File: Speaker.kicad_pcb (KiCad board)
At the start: 2 copper layers, 66 parts, among them J1 USB_C_Receptacle_USB2.0_16P, SW1 SW_Push, SW2 Volume Up, SW3 Volume Down, SW4 Play/Pause, SW5 Power Switch, U1 TPS61088RHLT, U2 MCP73871, U3 AP2112K-3.3, U4 MAX17048G_T10, U5 USBLC6-2SC6, U6 CH340X, U7 ESP32-WROOM-32, U8 MAX98357A

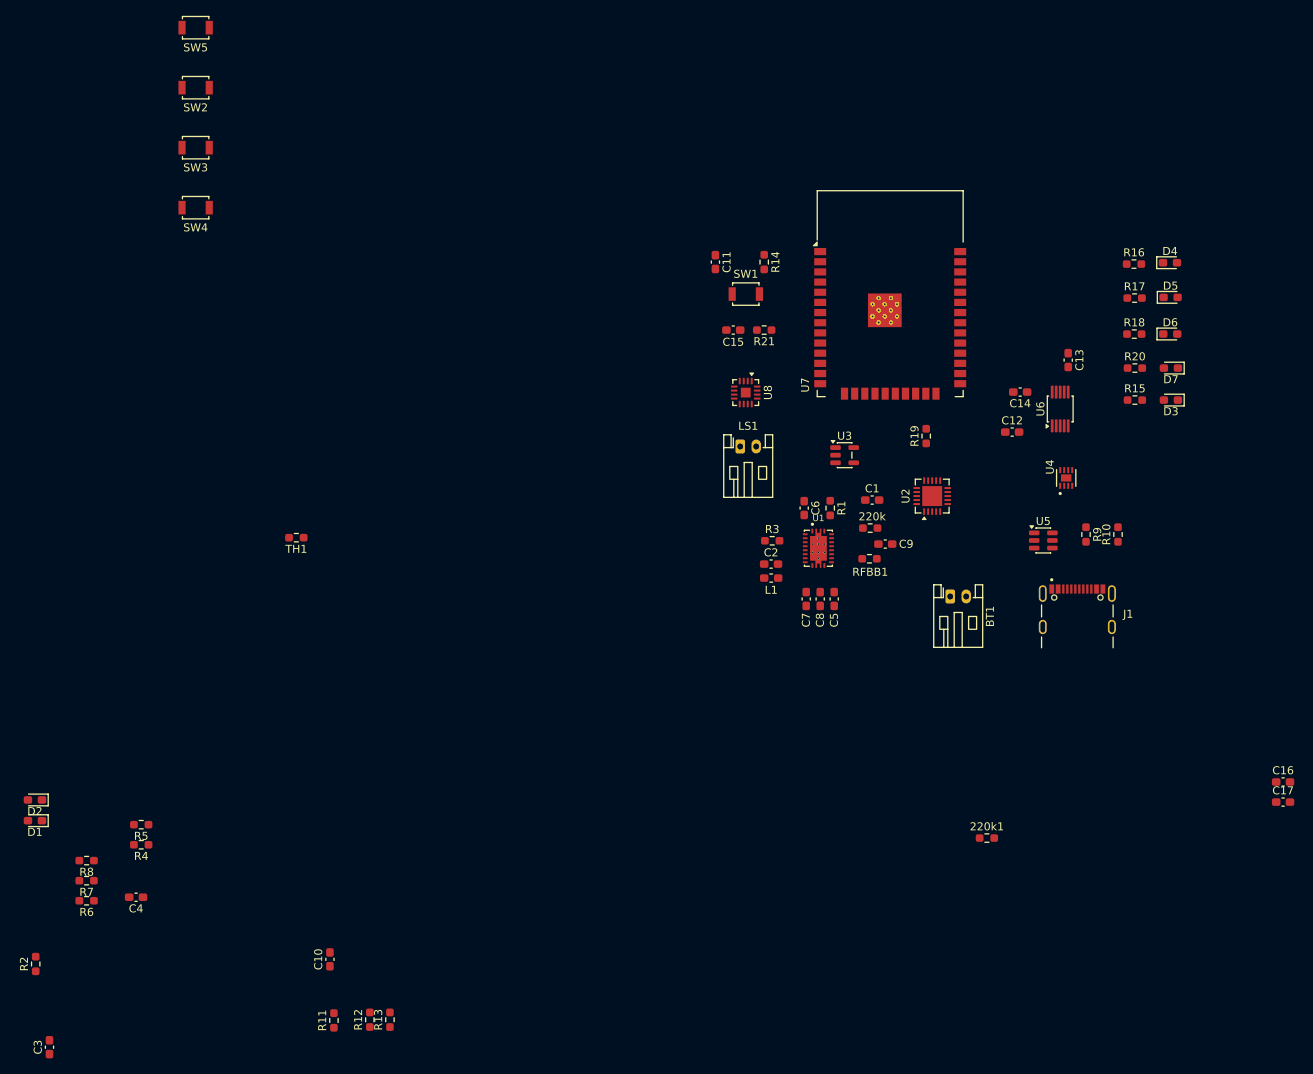
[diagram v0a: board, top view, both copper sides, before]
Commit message: Update the USB-C symbol to match the actual part
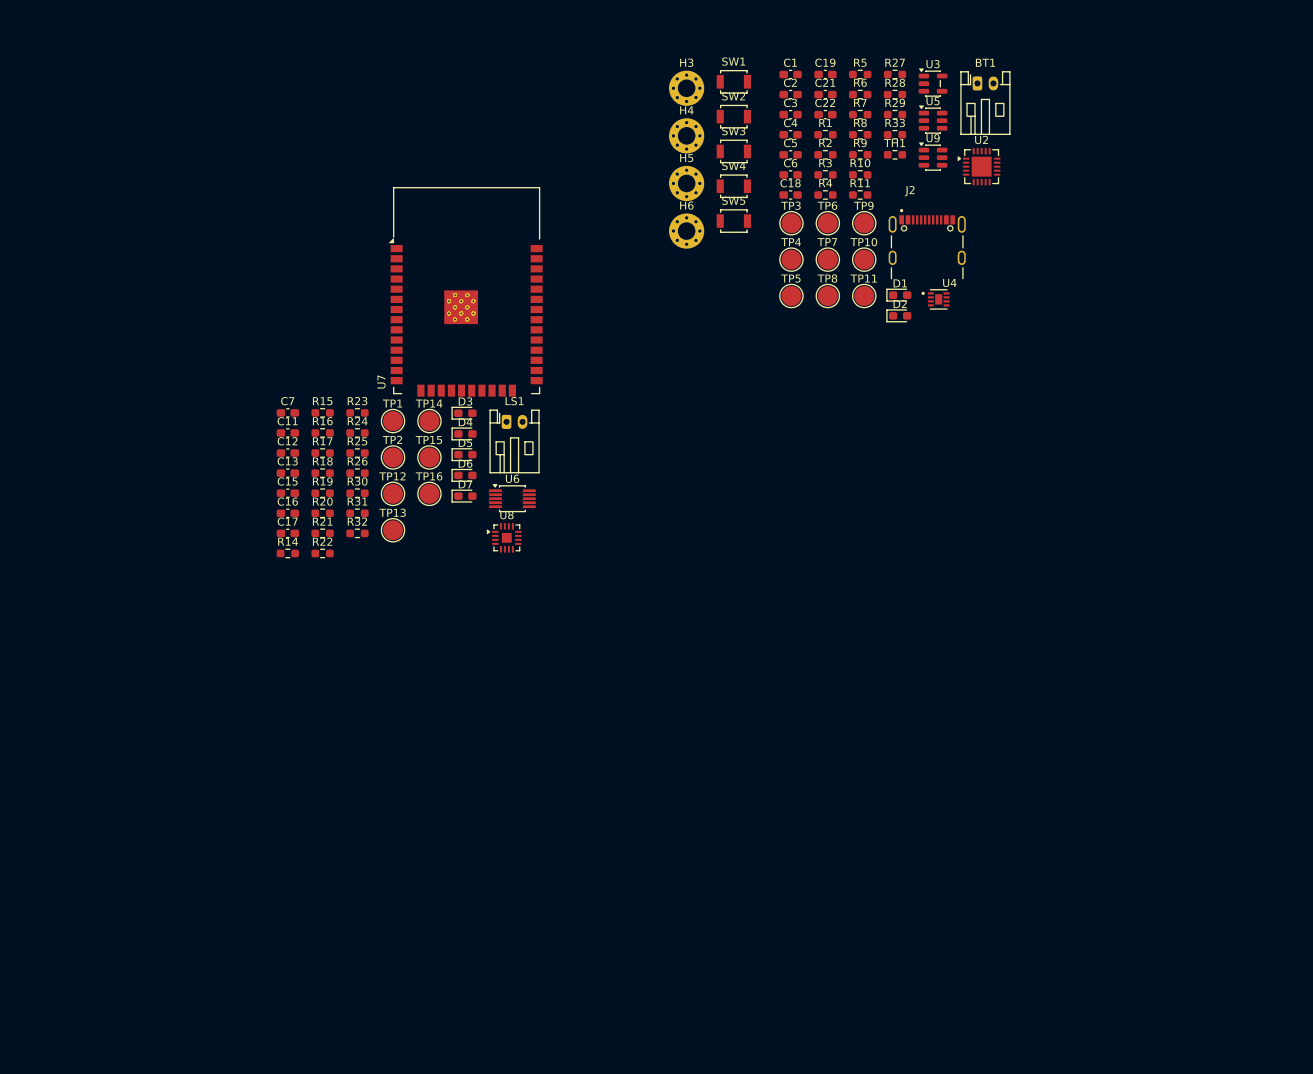
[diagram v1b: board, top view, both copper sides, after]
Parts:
- removed 220k, 220k1: RFB, Resistor_SMD:R_0603_1608Metric_Pad0.98x0.95mm_HandSolder
- removed C10: 100nF, Capacitor_SMD:C_0603_1608Metric_Pad1.08x0.95mm_HandSolder
- removed C14, C8: 0.1uF, Capacitor_SMD:C_0603_1608Metric_Pad1.08x0.95mm_HandSolder
- removed C9: 47uF, Capacitor_SMD:C_0603_1608Metric_Pad1.08x0.95mm_HandSolder
- removed J1: USB_C_Receptacle_USB2.0_16P, UJ20-C-H-G-SMT-1-P16-TR:SAMESKY_UJ20-C-H-G-SMT-1-P16-TR
- removed L1: 1.2uH, Inductor_SMD:L_0603_1608Metric_Pad1.05x0.95mm_HandSolder
- removed R12, R13: 5.1k, Resistor_SMD:R_0603_1608Metric_Pad0.98x0.95mm_HandSolder
- removed RFBB1: 70k, Resistor_SMD:R_0603_1608Metric_Pad0.98x0.95mm_HandSolder
- removed U1: TPS61088RHLT, TPS61088RHLT:IC_MSP430FR2522IRHLR
- added C18: 1uF, Capacitor_SMD:C_0603_1608Metric_Pad1.08x0.95mm_HandSolder, F.Cu at (128.3, 66.8)
- added C19: 1uF, Capacitor_SMD:C_0603_1608Metric_Pad1.08x0.95mm_HandSolder, F.Cu at (132.7, 51.7)
- added C21: 100pF, Capacitor_SMD:C_0603_1608Metric_Pad1.08x0.95mm_HandSolder, F.Cu at (132.7, 54.2)
- added C22: 100nF, Capacitor_SMD:C_0603_1608Metric_Pad1.08x0.95mm_HandSolder, F.Cu at (132.7, 56.8)
- added H3: MountingHole, MountingHole:MountingHole_2.2mm_M2_Pad_Via, F.Cu at (115.3, 53.5)
- added H4: MountingHole, MountingHole:MountingHole_2.2mm_M2_Pad_Via, F.Cu at (115.3, 59.4)
- added H5: MountingHole, MountingHole:MountingHole_2.2mm_M2_Pad_Via, F.Cu at (115.3, 65.4)
- added H6: MountingHole, MountingHole:MountingHole_2.2mm_M2_Pad_Via, F.Cu at (115.3, 71.3)
- added J2: UJ20-C-H-G-SMT-1-P16-TR, UJ20-C-H-G-SMT-1-P16-TR:SAMESKY_UJ20-C-H-G-SMT-1-P16-TR, F.Cu at (145.4, 77.3)
- added R22: 0, Resistor_SMD:R_0603_1608Metric_Pad0.98x0.95mm_HandSolder, F.Cu at (69.8, 111.6)
- added R23: 0, Resistor_SMD:R_0603_1608Metric_Pad0.98x0.95mm_HandSolder, F.Cu at (74.2, 94.0)
- added R24: 0, Resistor_SMD:R_0603_1608Metric_Pad0.98x0.95mm_HandSolder, F.Cu at (74.2, 96.5)
- added R25: 0, Resistor_SMD:R_0603_1608Metric_Pad0.98x0.95mm_HandSolder, F.Cu at (74.2, 99.1)
- added R26: 0, Resistor_SMD:R_0603_1608Metric_Pad0.98x0.95mm_HandSolder, F.Cu at (74.2, 101.6)
- added R27: 0, Resistor_SMD:R_0603_1608Metric_Pad0.98x0.95mm_HandSolder, F.Cu at (141.4, 51.7)
- added R28: 0, Resistor_SMD:R_0603_1608Metric_Pad0.98x0.95mm_HandSolder, F.Cu at (141.4, 54.2)
- added R29: 0, Resistor_SMD:R_0603_1608Metric_Pad0.98x0.95mm_HandSolder, F.Cu at (141.4, 56.8)
- added R30: 0, Resistor_SMD:R_0603_1608Metric_Pad0.98x0.95mm_HandSolder, F.Cu at (74.2, 104.1)
- added R31: 0, Resistor_SMD:R_0603_1608Metric_Pad0.98x0.95mm_HandSolder, F.Cu at (74.2, 106.6)
- added R32: 0, Resistor_SMD:R_0603_1608Metric_Pad0.98x0.95mm_HandSolder, F.Cu at (74.2, 109.1)
- added R33: 5.1k, Resistor_SMD:R_0603_1608Metric_Pad0.98x0.95mm_HandSolder, F.Cu at (141.4, 59.3)
- added TP1: TP_UART_TX, TestPoint:TestPoint_Pad_D2.5mm, F.Cu at (78.6, 95.1)
- added TP10: TP_VREG3.3, TestPoint:TestPoint_Pad_D2.5mm, F.Cu at (137.5, 74.9)
- added TP11: TP_VSYS_LDO, TestPoint:TestPoint_Pad_D2.5mm, F.Cu at (137.5, 79.4)
- added TP12: TP_D-, TestPoint:TestPoint_Pad_D2.5mm, F.Cu at (78.6, 104.2)
- added TP13: TP_D+, TestPoint:TestPoint_Pad_D2.5mm, F.Cu at (78.6, 108.7)
- added TP14: TP_DIN, TestPoint:TestPoint_Pad_D2.5mm, F.Cu at (83.2, 95.1)
- added TP15: TP_DIN, TestPoint:TestPoint_Pad_D2.5mm, F.Cu at (83.2, 99.6)
- added TP16: TP_BCLK, TestPoint:TestPoint_Pad_D2.5mm, F.Cu at (83.2, 104.2)
- added TP2: TP_UART_RX, TestPoint:TestPoint_Pad_D2.5mm, F.Cu at (78.6, 99.6)
- added TP3: TP_Charging, TestPoint:TestPoint_Pad_D2.5mm, F.Cu at (128.4, 70.3)
- added TP4: TP_VSYS, TestPoint:TestPoint_Pad_D2.5mm, F.Cu at (128.4, 74.9)
- added TP5: TP_VDD, TestPoint:TestPoint_Pad_D2.5mm, F.Cu at (128.4, 79.4)
- added TP6: TP_VBAT+, TestPoint:TestPoint_Pad_D2.5mm, F.Cu at (133.0, 70.3)
- added TP7: TP_FG_SDA, TestPoint:TestPoint_Pad_D2.5mm, F.Cu at (133.0, 74.9)
- added TP8: TP_FG_SCL, TestPoint:TestPoint_Pad_D2.5mm, F.Cu at (133.0, 79.4)
- added TP9: TP_FG_ALRT, TestPoint:TestPoint_Pad_D2.5mm, F.Cu at (137.5, 70.3)
- added U9: USBLC6-2SC6, Package_TO_SOT_SMD:SOT-23-6, F.Cu at (146.1, 62.1)
- C1: value 39pF -> 1uF
- C2: value 0.1uF -> 100pF
- C3: value 1nF -> 100nF
- C4: value 4.7u -> 4.7uF
- C5: value 47nF -> 4.7uF
- C6: value 2.2uF -> 0.1uF
- C7: value 10uF -> 0.1uF
- R1: value 23.7k -> 330k
- R2: value 243K -> 110k
- R3: value 322K -> 5.1k
- R5: value 5k -> 10k
- R6: value 10k -> 470
- moved C3 148.9 mm to (128.3, 56.8), turned to 0 degrees
- moved R2 141.3 mm to (132.7, 61.8), turned to 0 degrees
- moved R6 139.7 mm to (137.0, 54.2), turned to 0 degrees
- moved R7 136.1 mm to (137.0, 56.8), turned to 0 degrees
- moved R8 132.6 mm to (137.0, 59.3), turned to 0 degrees
- moved R5 129.9 mm to (137.0, 51.7), turned to 0 degrees
- moved C16 128.9 mm to (65.5, 106.6)
- moved C17 128.9 mm to (65.5, 109.1)
- moved D1 126.5 mm to (142.0, 79.3), turned to 0 degrees
- moved C4 125.6 mm to (128.3, 59.3), turned to 0 degrees
- moved D2 123.9 mm to (142.0, 81.9), turned to 0 degrees
- moved R11 122.4 mm to (137.0, 66.8), turned to 0 degrees
- moved R4 117.9 mm to (132.7, 66.8), turned to 0 degrees
- moved R16 103.6 mm to (69.8, 96.5)
- moved R17 103.3 mm to (69.8, 99.1)
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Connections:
- C1 pad 1: Net-(U1-COMP) -> GND
- C1 pad 2: GND -> VDD
- C16 pad 2: VREG_5V -> VREG_3.3V
- C17 pad 2: VREG_5V -> VREG_3.3V
- C2 pad 1: Net-(C2-Pad1) -> GND
- C2 pad 2: Net-(U1-BOOT) -> VDD
- C3 pad 1: Net-(C3-Pad1) -> GND
- C3 pad 2: GND -> VDD
- C5 pad 1: Net-(U1-SS) -> VSYS
- C6 pad 1: GND -> VBAT+
- C6 pad 2: Net-(U1-VCC) -> GND
- C7 pad 2: VSYS -> VREG_3.3V
- D1 pad 2: Net-(D1-A) -> VDD
- D2 pad 2: Net-(D2-A) -> VDD
- R1 pad 1: Net-(U1-COMP) -> VDD
- R1 pad 2: Net-(C3-Pad1) -> Net-(U2-VPCC)
- R2 pad 1: Net-(U1-ILIM) -> GND
- R2 pad 2: GND -> Net-(U2-VPCC)
- R3 pad 1: Net-(C2-Pad1) -> GND
- R7 pad 1: Net-(D1-A) -> Net-(U2-STAT1/~{LBO})
- R7 pad 2: VREG_3.3V -> Net-(D1-K)
- R8 pad 1: Net-(D2-A) -> Net-(U2-STAT2)
- R8 pad 2: VREG_3.3V -> Net-(D2-K)
- U2 pad 2: VDD -> Net-(U2-VPCC)
- U2 pad 7: Net-(D2-K) -> Net-(U2-STAT2)
- U2 pad 8: Net-(D1-K) -> Net-(U2-STAT1/~{LBO})
- U3 pad 1: VREG_5V -> VSYS
- U3 pad 3: VREG_5V -> VSYS
- U4 pad 3: VREG_3.3V -> VBAT+
- U6 pad 1: D+ -> Net-(U6-UD+)
- U6 pad 2: D- -> Net-(U6-UD-)
- U6 pad 7: VREG_5V -> Net-(U6-V3)
- U7 pad 9: unconnected-(U7-IO33-Pad9) -> /MCU/AMP_SDM
- U8 pad 4: unconnected-(U8-~{SD_MODE}-Pad4) -> /MCU/AMP_SDM
- U8 pad 7: VREG_5V -> VREG_3.3V
- U8 pad 8: VREG_5V -> VREG_3.3V

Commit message: Put component families together on PCB
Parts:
- added C8: 1nF, Capacitor_SMD:C_0603_1608Metric_Pad1.08x0.95mm_HandSolder, F.Cu at (70.0, 38.6)
- TP1, TP10, TP11, TP12, TP13, TP14, TP15, TP16, TP2, TP3, TP4, TP5, TP6, TP7, TP8, TP9: footprint TestPoint:TestPoint_Pad_D2.5mm -> TestPoint:TestPoint_Pad_D1.5mm
- moved R20 198.7 mm to (259.5, 47.6)
- moved R18 196.9 mm to (259.8, 49.9), turned to 180 degrees
- moved R17 195.6 mm to (259.8, 52.4), turned to 180 degrees
- moved R16 194.5 mm to (259.8, 54.9), turned to 180 degrees
- moved R15 193.4 mm to (259.8, 57.4), turned to 180 degrees
- moved D7 184.8 mm to (263.5, 47.6), turned to 180 degrees
- moved D6 183.4 mm to (263.5, 49.6), turned to 180 degrees
- moved D5 182.0 mm to (263.5, 52.2), turned to 180 degrees
- moved D4 180.7 mm to (263.5, 54.8), turned to 180 degrees
- moved D3 179.6 mm to (263.5, 57.4), turned to 180 degrees
- moved R19 175.9 mm to (240.8, 62.9), turned to -90 degrees
- moved R14 170.4 mm to (221.8, 43.8), turned to -90 degrees
- moved C11 166.8 mm to (223.6, 43.7), turned to -90 degrees
- moved R21 162.7 mm to (221.9, 51.2), turned to 180 degrees
- moved C15 161.6 mm to (218.1, 51.2), turned to 180 degrees
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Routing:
- net VREG_3.3V: track 0.00 -> 17.5 mm
- net VDD: track 0.00 -> 13.8 mm
- net VSYS: track 0.00 -> 12.1 mm
- net Net-(U9-VBUS): track 0.00 -> 9.81 mm
- net Net-(J2-D2_P): track 0.00 -> 9.34 mm
- net Net-(J2-D2_N): track 0.00 -> 9.05 mm
- net Net-(U4-SCL): track 0.00 -> 8.90 mm
- net Net-(U6-TXD): track 0.00 -> 8.53 mm
- net Net-(U4-SDA): track 0.00 -> 6.69 mm
- net Net-(U4-~{ALERT}): track 0.00 -> 6.26 mm
- net Net-(U6-UD-): track 0.00 -> 5.62 mm
- net Net-(U6-UD+): track 0.00 -> 5.46 mm
- net Net-(U6-RXD): track 0.00 -> 5.40 mm
- net Net-(U6-V3): track 0.00 -> 5.33 mm
- net Net-(U2-VPCC): track 0.00 -> 5.15 mm
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
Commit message: PCB Design before inter-family routing
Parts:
- moved J2 222.8 mm to (244.5, 94.1), turned to 0 degrees
- moved TP5 218.1 mm to (248.2, 83.9), turned to -90 degrees
- moved R33 215.0 mm to (246.2, 82.9), turned to 90 degrees
- moved R3 210.7 mm to (242.4, 82.9), turned to -90 degrees
- moved U5 209.6 mm to (244.3, 78.9), turned to 90 degrees
- moved U9 206.9 mm to (239.2, 82.7), turned to 90 degrees
- moved C1 203.2 mm to (238.2, 79.7), turned to 0 degrees
- moved C2 201.9 mm to (238.2, 78.1), turned to 0 degrees
- moved C3 200.5 mm to (238.2, 76.5), turned to 0 degrees
- moved D2 166.4 mm to (230.2, 78.5), turned to 0 degrees
- moved D1 165.3 mm to (230.2, 76.7), turned to 0 degrees
- moved R6 163.0 mm to (226.7, 79.9), turned to 0 degrees
- moved R8 161.9 mm to (226.7, 78.3), turned to 0 degrees
- moved TP3 161.1 mm to (228.1, 74.3), turned to -90 degrees
- moved R7 160.8 mm to (226.7, 76.7), turned to 0 degrees
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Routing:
- net Net-(U7-IO32): track 0.00 -> 1.85 mm
- net Net-(C15-Pad1): track 0.00 -> 1.62 mm

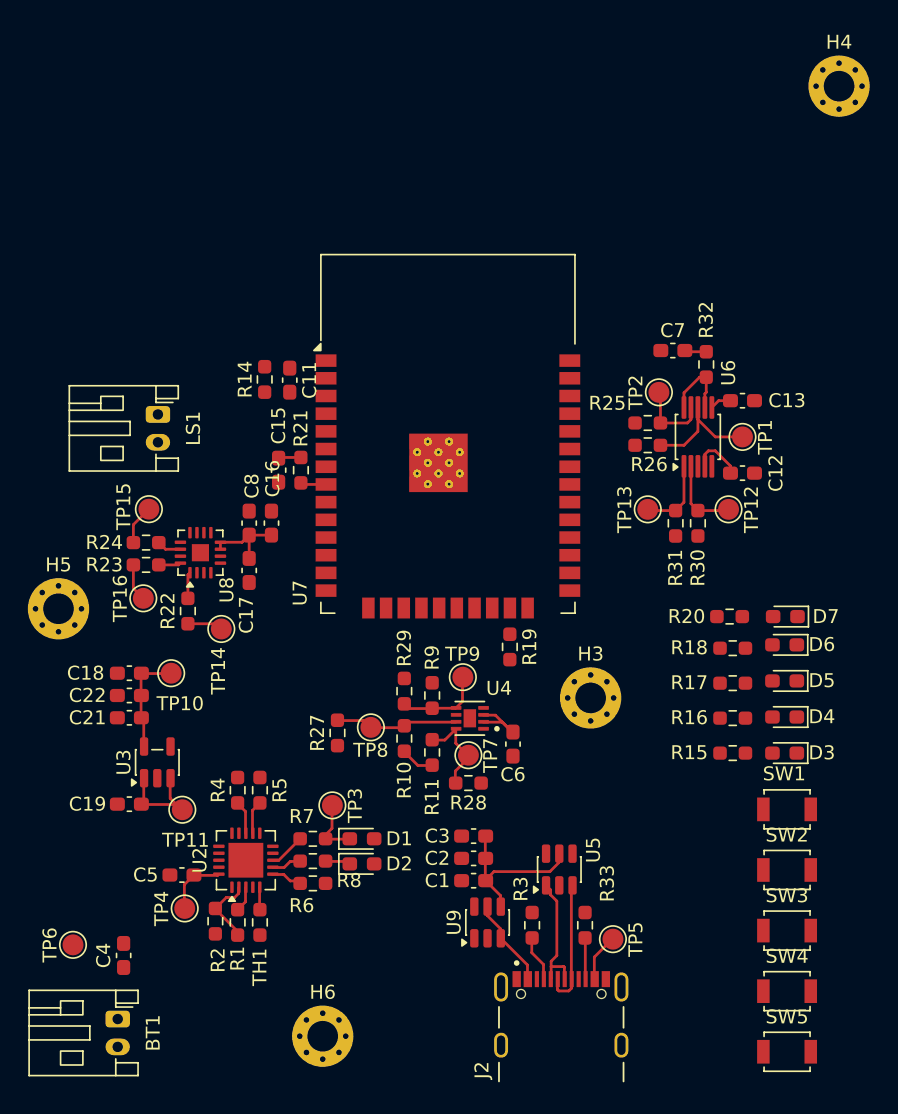
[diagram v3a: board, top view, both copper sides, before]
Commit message: Board shape setup
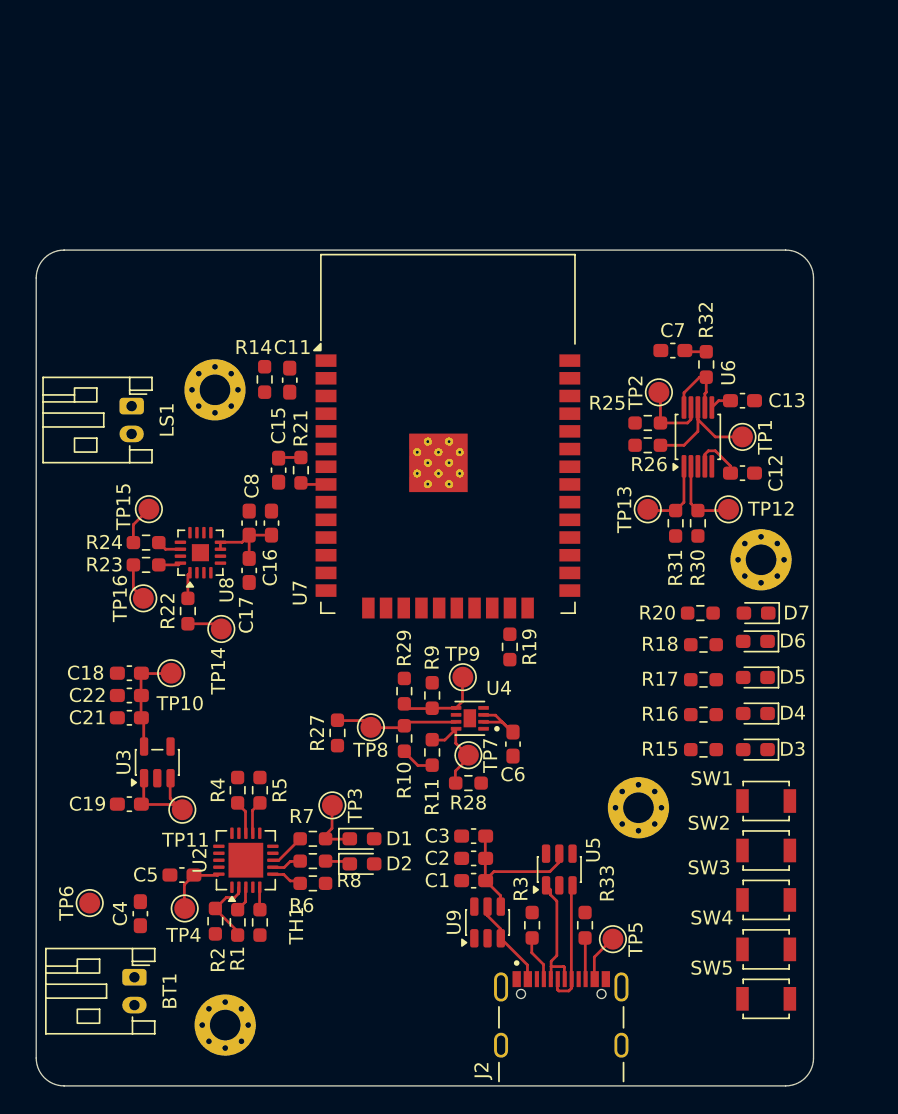
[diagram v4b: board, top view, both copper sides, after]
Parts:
- moved H4 34.5 mm to (258.8, 56.6)
- moved H5 19.3 mm to (219.6, 44.4)
- moved H3 8.60 mm to (250.0, 74.4)
- moved H6 7.05 mm to (220.4, 90.0)
- moved SW5 4.09 mm to (259.2, 88.2)
- moved SW4 3.35 mm to (259.2, 84.6)
- moved C4 3.23 mm to (214.3, 82.0)
- moved BT1 3.23 mm to (213.8, 86.6)
- moved TP6 3.23 mm to (210.6, 81.3)
- moved SW3 2.66 mm to (259.2, 81.0)
- moved R15 2.11 mm to (254.7, 70.3)
- moved R16 2.11 mm to (254.7, 67.8)
- moved R17 2.11 mm to (254.7, 65.2)
- moved R18 2.11 mm to (254.7, 62.7)
- moved R20 2.11 mm to (254.5, 60.5)
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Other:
- board outline added: 55.8 x 60 mm
- board text added: "Made by John Denny Rev 1 (Sep 2026)"
